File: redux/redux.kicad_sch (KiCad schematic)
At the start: 251 parts, among them J14 Backplane, J3 Common, J4 Ext-2, J5 Ext-1, J6 Master, J7 Ext+1, J8 Ext+2, M1000 Bracket, Q1 MMBT3906, U1 MC100LVEL16, U13 MC100LVEL14, U15 SY89421V, U16 LM311, U34 AD7841, U44 AD586, U45 AD586, U62 LT1086-ADJ, U63 LT1086-ADJ, U64 16715-89002, U65 74CBT3125, U66 SG-615P 19.6608MHz, U67 SN74FB2040, U68 MC100LVEL11, U73 MC100LVEL16, U74 MC10EL34, U75 PCF8584, U76 74ABT540, U79 NEL HS-2810 101MHz

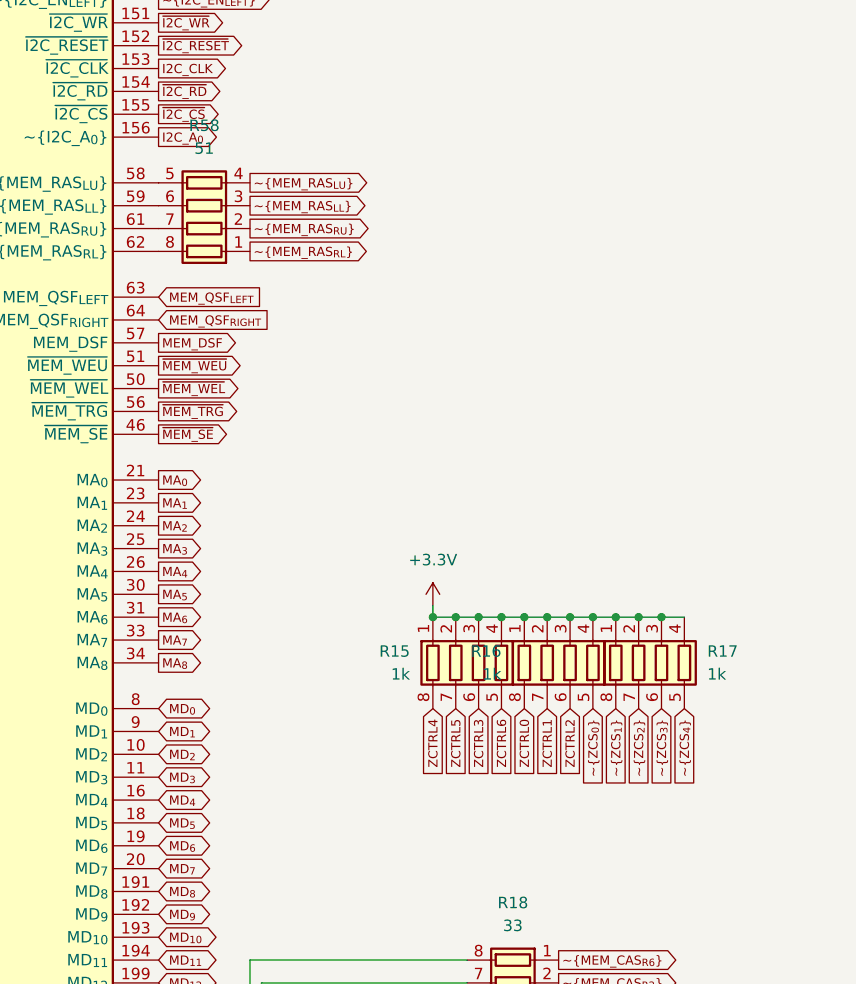
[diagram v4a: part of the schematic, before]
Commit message: Clean up FPGA, zoom CS routing
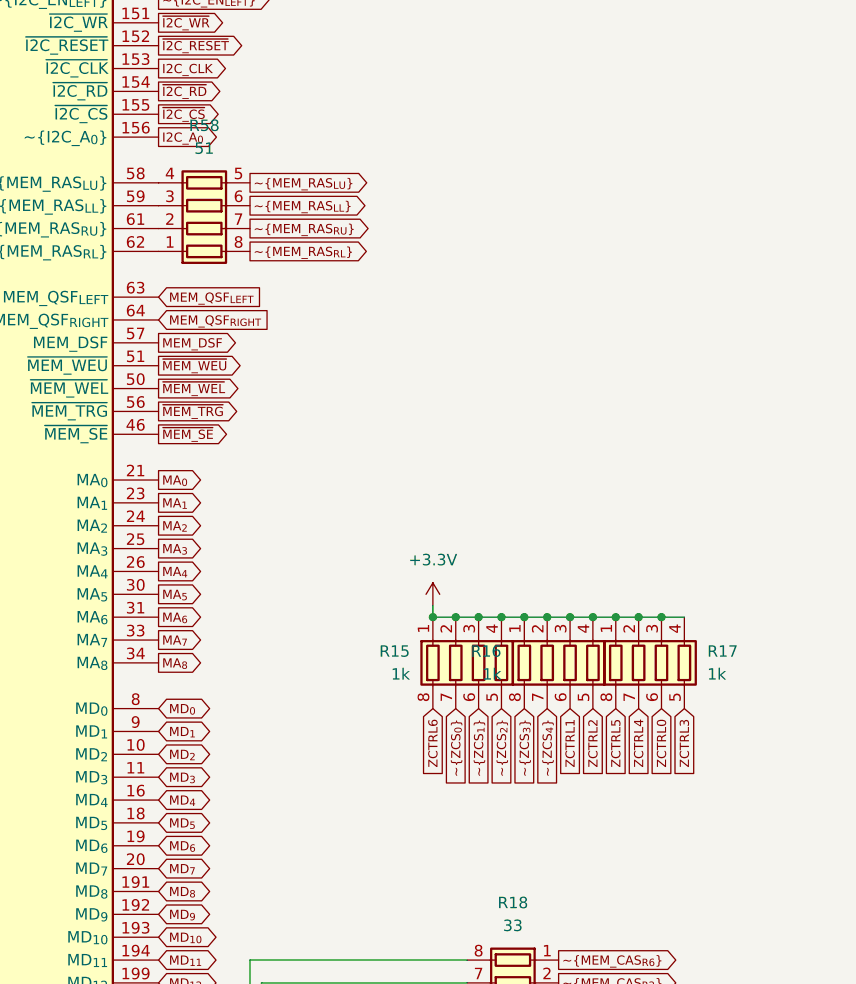
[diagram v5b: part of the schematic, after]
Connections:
- net ZCTRL0: now also R17.6 (R3.2); no longer R16.8 (R1.2)
- net ZCTRL1: now also R16.6 (R3.2); no longer R16.7 (R2.2)
- net ZCTRL2: now also R16.5 (R4.2); no longer R16.6 (R3.2)
- net ZCTRL3: now also R17.5 (R4.2); no longer R15.6 (R3.2)
- net ZCTRL4: now also R17.7 (R2.2); no longer R15.8 (R1.2)
- net ZCTRL5: now also R17.8 (R1.2); no longer R15.7 (R2.2)
- net ZCTRL6: now also R15.8 (R1.2); no longer R15.5 (R4.2)
- net ~{MEM_RAS_{LL}}: now also R58.6 (R3.2); no longer R58.3 (R3.1)
- net ~{MEM_RAS_{LU}}: now also R58.5 (R4.2); no longer R58.4 (R4.1)
- net ~{MEM_RAS_{RL}}: now also R58.8 (R1.2); no longer R58.1 (R1.1)
- net ~{MEM_RAS_{RU}}: now also R58.7 (R2.2); no longer R58.2 (R2.1)
- net ~{ZCS_{0}}: now also R15.7 (R2.2); no longer R16.5 (R4.2)
- net ~{ZCS_{1}}: now also R15.6 (R3.2); no longer R17.8 (R1.2)
- net ~{ZCS_{2}}: now also R15.5 (R4.2); no longer R17.7 (R2.2)
- net ~{ZCS_{3}}: now also R16.8 (R1.2); no longer R17.6 (R3.2)
- net ~{ZCS_{4}}: now also R16.7 (R2.2); no longer R17.5 (R4.2)
- net at U64.58 (~{MEM_RAS_{LU}}): now also R58.4 (R4.1); no longer R58.5 (R4.2)
- net at U64.59 (~{MEM_RAS_{LL}}): now also R58.3 (R3.1); no longer R58.6 (R3.2)
- net at U64.61 (~{MEM_RAS_{RU}}): now also R58.2 (R2.1); no longer R58.7 (R2.2)
- net at U64.62 (~{MEM_RAS_{RL}}): now also R58.1 (R1.1); no longer R58.8 (R1.2)
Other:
- moved on the sheet: R58
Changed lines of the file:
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@@
 	(global_label "ZCTRL2"
 		(shape input)
-		(at 638.81 262.89 270)
+		(at 641.35 262.89 270)
 		(fields_autoplaced yes)
 		(effects
@@
 		)
 		(property "Intersheetrefs" "${INTERSHEET_REFS}"
-			(at 638.81 270.8417 90)
+			(at 641.35 270.8417 90)
 			(effects
 				(font
@@
 	(global_label "ZCTRL3"
 		(shape input)
-		(at 628.65 262.89 270)
+		(at 651.51 262.89 270)
 		(fields_autoplaced yes)
 		(effects
@@
 		)
 		(property "Intersheetrefs" "${INTERSHEET_REFS}"
-			(at 628.65 270.8417 90)
+			(at 651.51 270.8417 90)
 			(effects
 				(font
@@
 	(global_label "~{ZCS_{0}}"
 		(shape input)
-		(at 641.35 262.89 270)
+		(at 626.11 262.89 270)
 		(fields_autoplaced yes)
 		(effects
@@
 		)
 		(property "Intersheetrefs" "${INTERSHEET_REFS}"
-			(at 641.35 269.0438 90)
+			(at 626.11 269.0438 90)
 			(effects
 				(font
@@
 	(global_label "ZCTRL6"
 		(shape input)
-		(at 631.19 262.89 270)
+		(at 623.57 262.89 270)
 		(fields_autoplaced yes)
 		(effects
@@
 		)
 		(property "Intersheetrefs" "${INTERSHEET_REFS}"
-			(at 631.19 270.8417 90)
+			(at 623.57 270.8417 90)
 			(effects
 				(font
@@
 	(global_label "ZCTRL0"
 		(shape input)
-		(at 633.73 262.89 270)
+		(at 648.97 262.89 270)
 		(fields_autoplaced yes)
 		(effects
@@
 		)
 		(property "Intersheetrefs" "${INTERSHEET_REFS}"
-			(at 633.73 270.8417 90)
+			(at 648.97 270.8417 90)
 			(effects
 				(font
@@
 	(global_label "ZCTRL5"
 		(shape input)
-		(at 626.11 262.89 270)
+		(at 643.89 262.89 270)
 		(fields_autoplaced yes)
 		(effects
@@
 		)
 		(property "Intersheetrefs" "${INTERSHEET_REFS}"
-			(at 626.11 270.8417 90)
+			(at 643.89 270.8417 90)
 			(effects
 				(font
@@
 	(global_label "ZCTRL1"
 		(shape input)
-		(at 636.27 262.89 270)
+		(at 638.81 262.89 270)
 		(fields_autoplaced yes)
 		(effects
@@
 		)
 		(property "Intersheetrefs" "${INTERSHEET_REFS}"
-			(at 636.27 270.8417 90)
+			(at 638.81 270.8417 90)
 			(effects
 				(font
@@
 	(global_label "~{ZCS_{2}}"
 		(shape input)
-		(at 646.43 262.89 270)
+		(at 631.19 262.89 270)
 		(fields_autoplaced yes)
 		(effects
@@
 		)
 		(property "Intersheetrefs" "${INTERSHEET_REFS}"
-			(at 646.43 269.0438 90)
+			(at 631.19 269.0438 90)
 			(effects
 				(font
@@
 	(global_label "ZCTRL4"
 		(shape input)
-		(at 623.57 262.89 270)
+		(at 646.43 262.89 270)
 		(fields_autoplaced yes)
 		(effects
@@
 		)
 		(property "Intersheetrefs" "${INTERSHEET_REFS}"
-			(at 623.57 270.8417 90)
+			(at 646.43 270.8417 90)
 			(effects
 				(font
@@
 	(global_label "~{ZCS_{4}}"
 		(shape input)
-		(at 651.51 262.89 270)
+		(at 636.27 262.89 270)
 		(fields_autoplaced yes)
 		(effects
@@
 		)
 		(property "Intersheetrefs" "${INTERSHEET_REFS}"
-			(at 651.51 269.0438 90)
+			(at 636.27 269.0438 90)
 			(effects
 				(font
@@
 	(global_label "~{ZCS_{1}}"
 		(shape input)
-		(at 643.89 262.89 270)
+		(at 628.65 262.89 270)
 		(fields_autoplaced yes)
 		(effects
@@
 		)
 		(property "Intersheetrefs" "${INTERSHEET_REFS}"
-			(at 643.89 269.0438 90)
+			(at 628.65 269.0438 90)
 			(effects
 				(font
@@
 	(global_label "~{ZCS_{3}}"
 		(shape input)
-		(at 648.97 262.89 270)
+		(at 633.73 262.89 270)
 		(fields_autoplaced yes)
 		(effects
@@
 		)
 		(property "Intersheetrefs" "${INTERSHEET_REFS}"
-			(at 648.97 269.0438 90)
+			(at 633.73 269.0438 90)
 			(effects
 				(font
@@
 	(symbol
 		(lib_id "Device:R_Pack04")
-		(at 598.17 207.01 90)
+		(at 598.17 207.01 270)
+		(mirror x)
 		(unit 1)
 		(exclude_from_sim no)

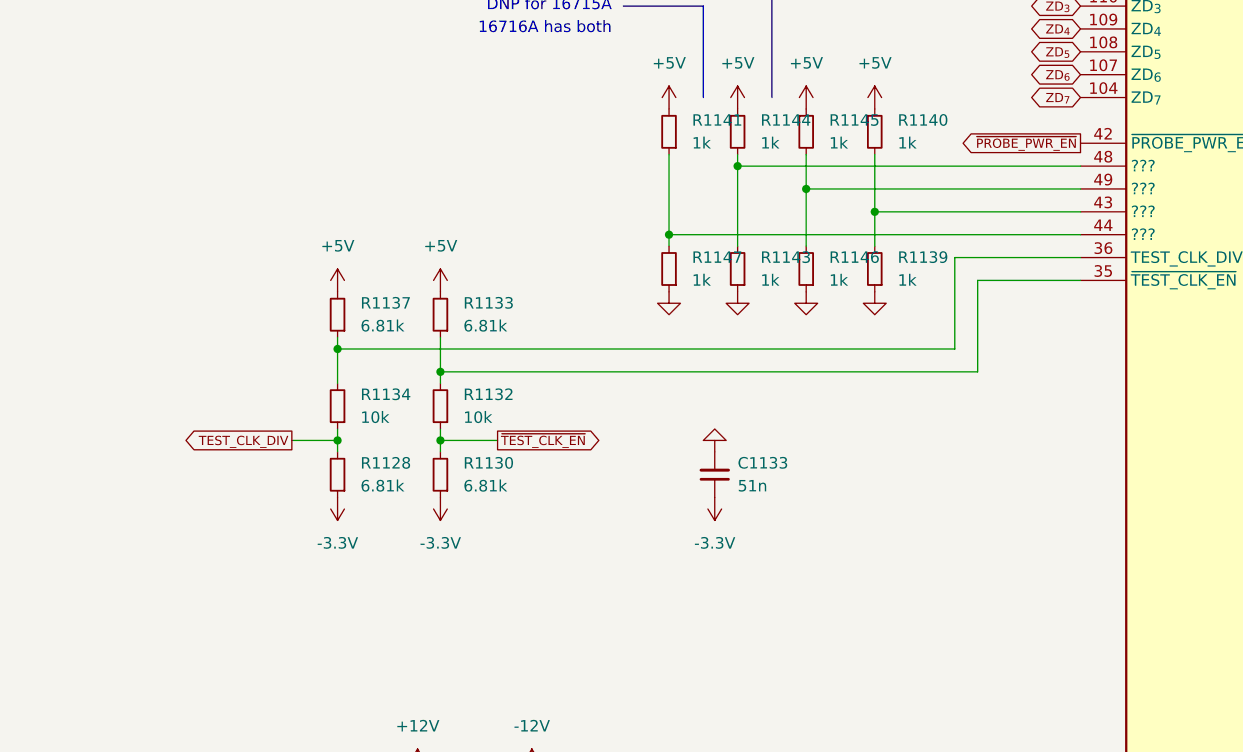
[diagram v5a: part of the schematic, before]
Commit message: improve routing around fpga
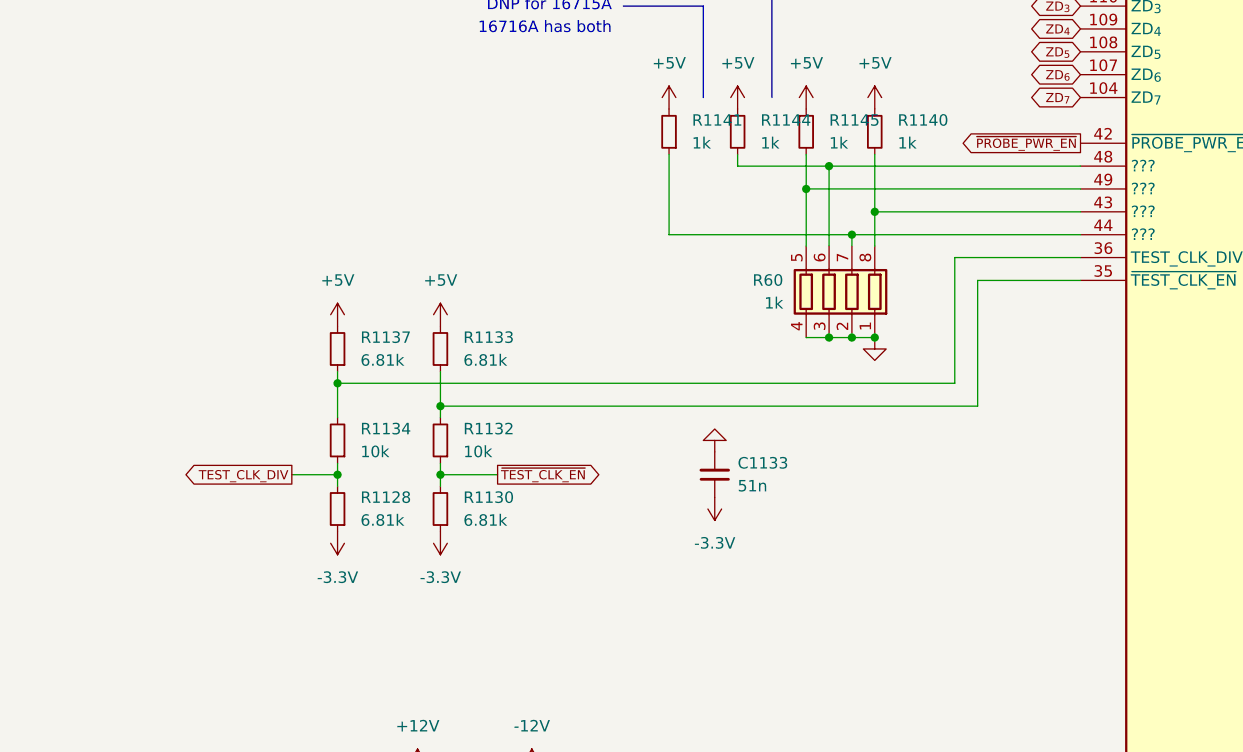
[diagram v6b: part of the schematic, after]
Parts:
- removed R1139, R1143, R1146, R1147: 1k, fp:R0805, symbol Device:R_Small
- added R60: 1k, fp:R_Array_Convex_4x0603, symbol Device:R_Pack04
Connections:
- net GND: now also R60.1 (R1.1), R60.2 (R2.1), R60.3 (R3.1), R60.4 (R4.1)
- net at R1140.2, U64.43 (???): now also R60.8 (R1.2)
- net at R1141.1, U64.44 (???): now also R60.7 (R2.2)
- net at R1144.2, U64.48 (???): now also R60.6 (R3.2)
- net at R1145.2, U64.49 (???): now also R60.5 (R4.2)
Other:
- moved on the sheet: R1128, R1130, R1132, R1133, R1134, R1137

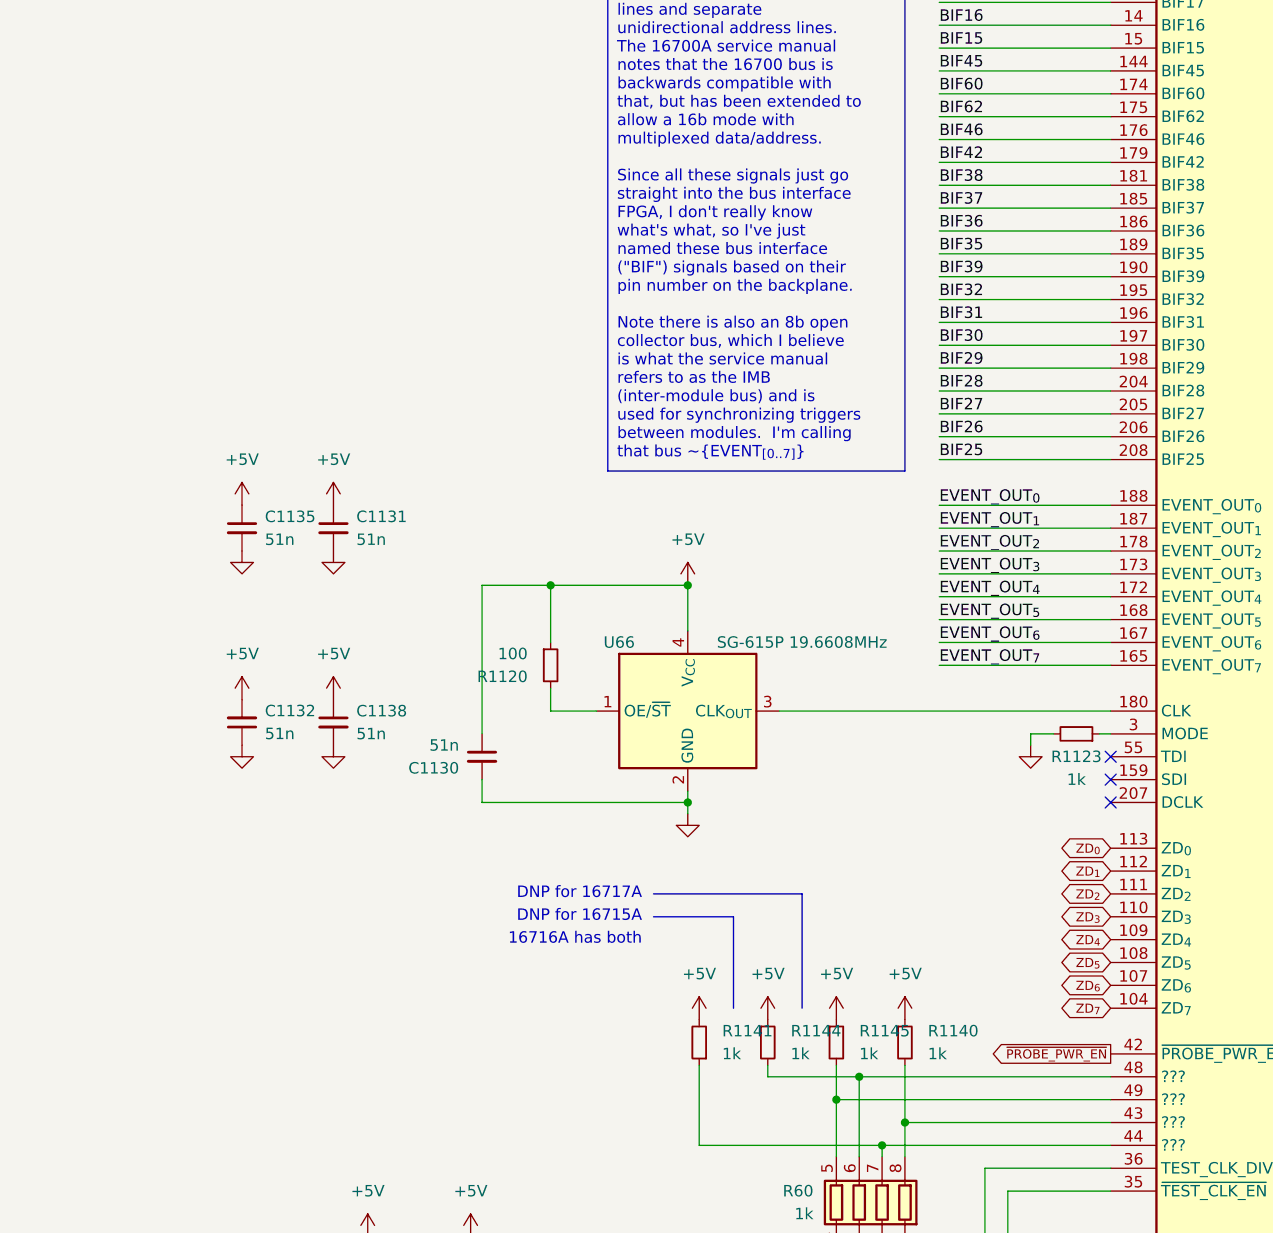
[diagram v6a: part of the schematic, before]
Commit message: Allow alternate footprints for FPGA oscillator
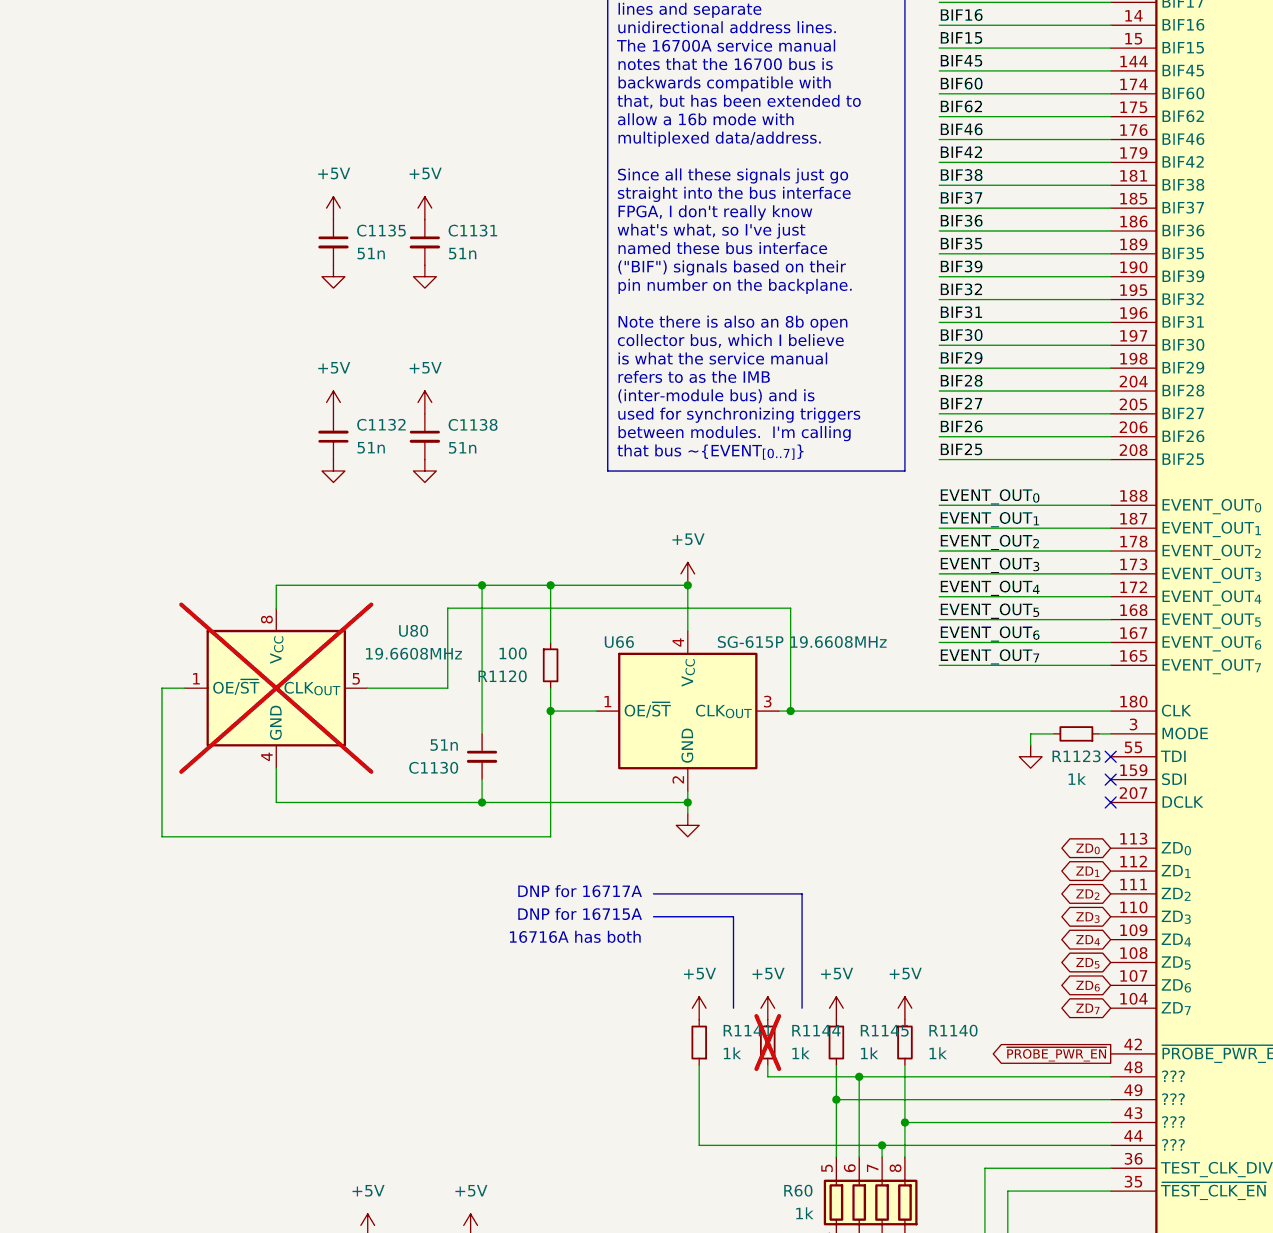
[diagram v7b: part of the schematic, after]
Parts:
- added U80: 19.6608MHz, Oscillator:Oscillator_DIP-8, symbol 16717a:Oscillator_DIP8
- R1144: now not fitted
- U66: footprint fp:SG-615P -> fp:SG-615P_ext
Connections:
- net +5V: now also U80.8 (V_{CC})
- net GND: now also U80.4 (GND)
- net at U64.180 (CLK), U66.3 (CLK_{OUT}): now also U80.5 (CLK_{OUT})
- net at R1120.2, U66.1 (OE/~{ST}): now also U80.1 (OE/~{ST})
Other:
- moved on the sheet: C1131, C1132, C1135, C1138
